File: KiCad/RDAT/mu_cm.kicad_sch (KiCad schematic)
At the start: 9 parts

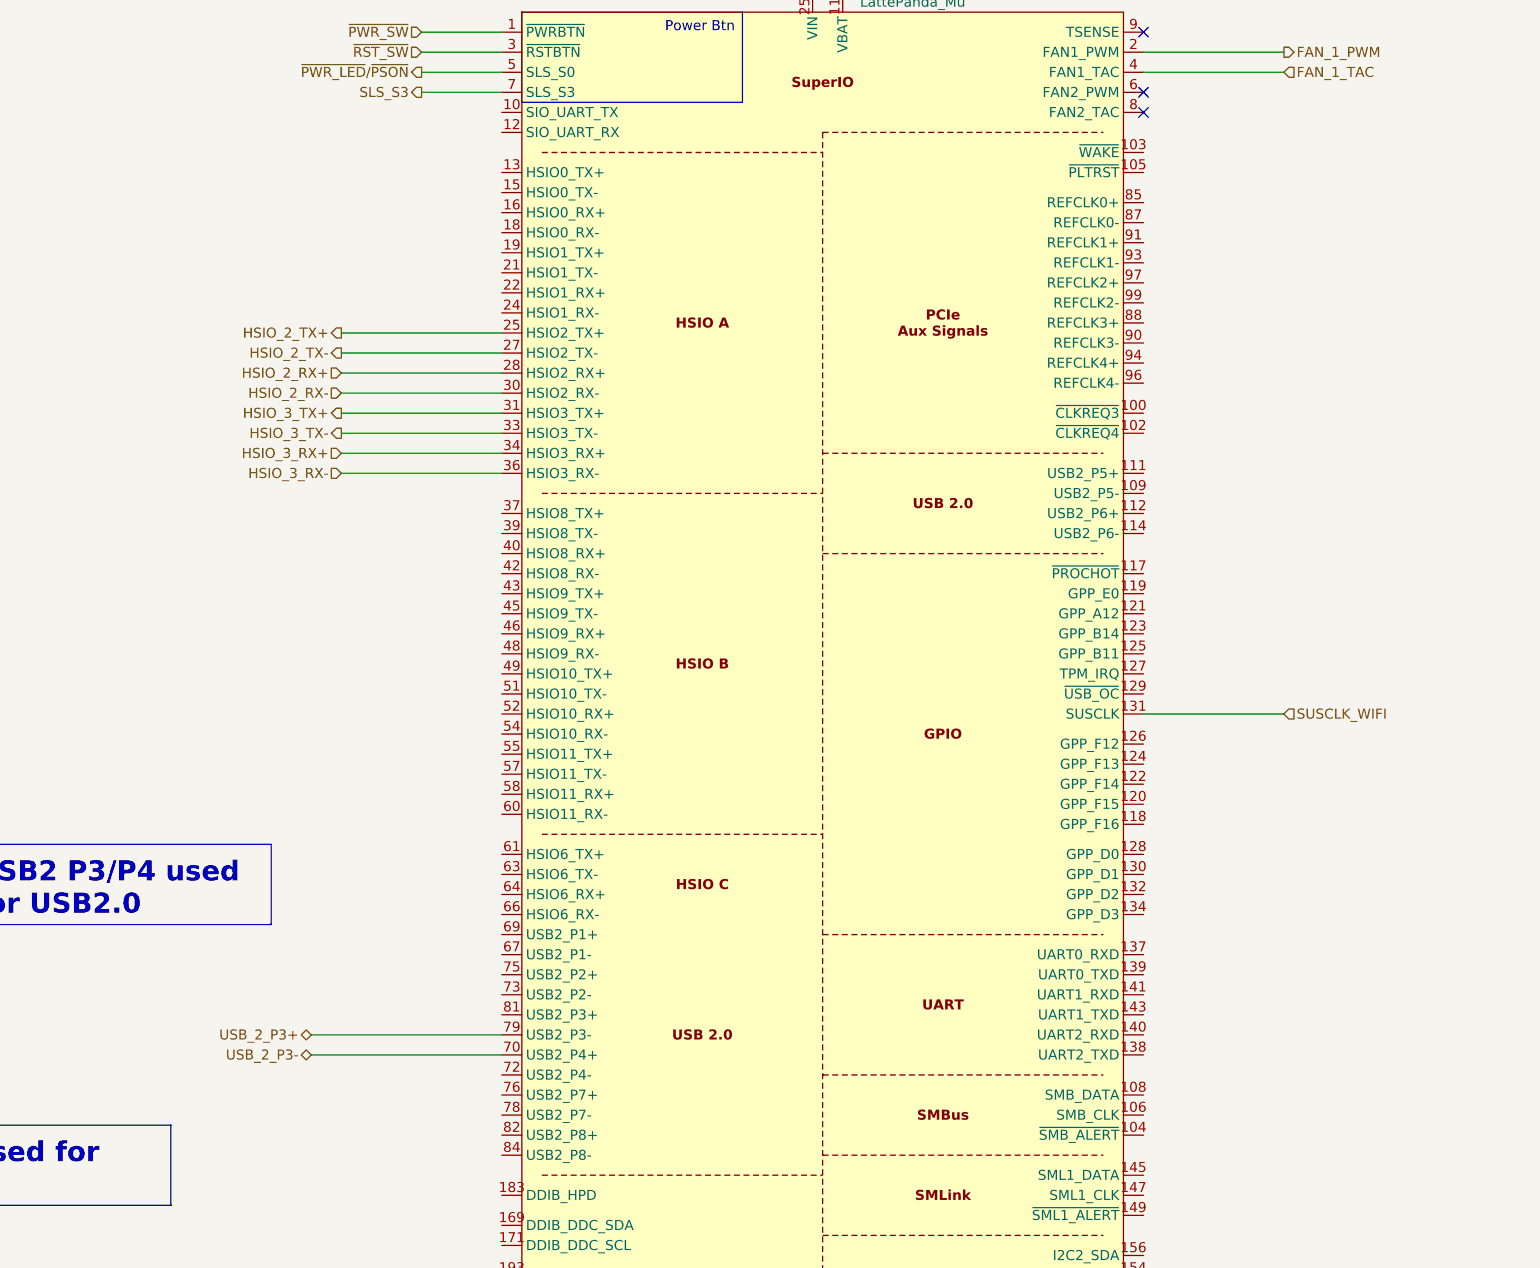
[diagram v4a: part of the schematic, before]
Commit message: Connected m.2 E Key
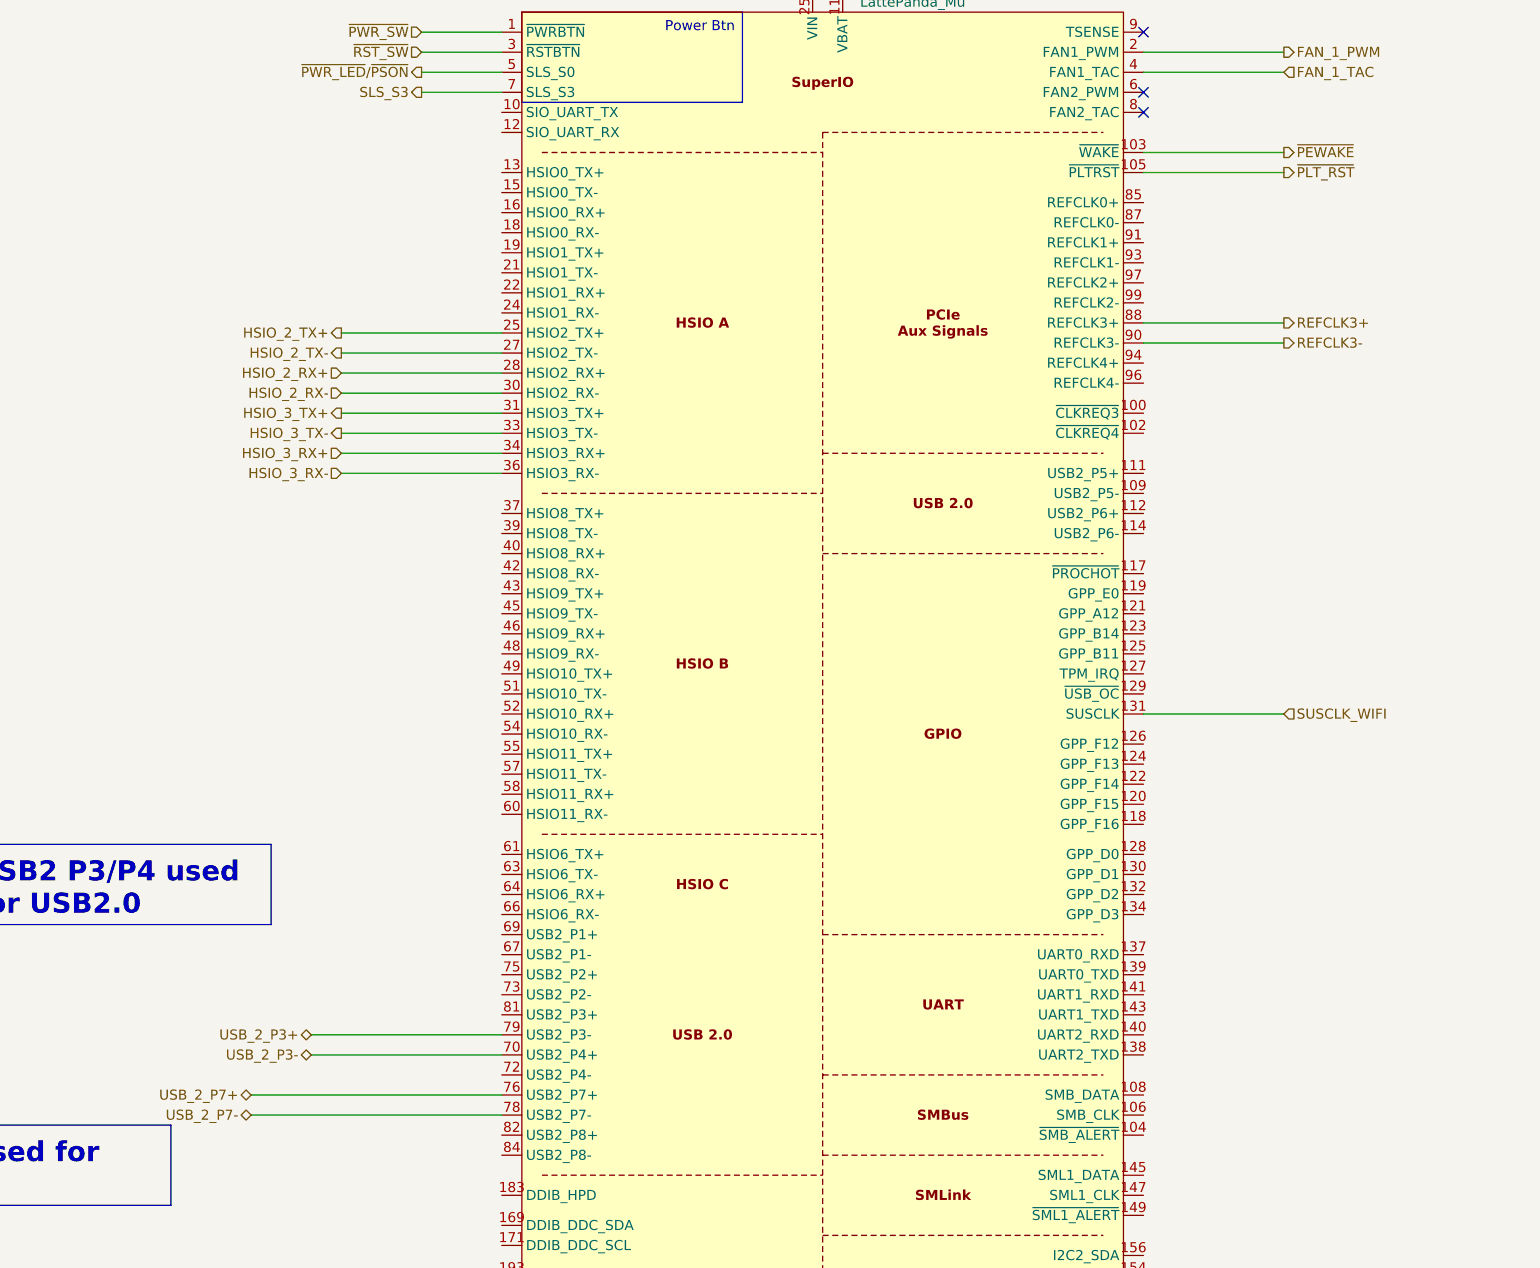
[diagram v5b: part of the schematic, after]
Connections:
- net ~{PEWAKE}: now reaches A1.103 (~{WAKE})
- net ~{PLT_RST}: now reaches A1.105 (~{PLTRST})
- net USB_2_P7+: now reaches A1.76 (USB2_P7+)
- net USB_2_P7-: now reaches A1.78 (USB2_P7-)
- net REFCLK3+: now reaches A1.88 (REFCLK3+)
- net REFCLK3-: now reaches A1.90 (REFCLK3-)
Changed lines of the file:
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@@
+	(wire
+		(pts
+			(xy 176.53 104.14) (xy 194.31 104.14)
+		)
+		(stroke
+			(width 0)
+			(type default)
+		)
+	)
 	(wire
 		(pts
@@
 	(wire
 		(pts
+			(xy 95.25 201.93) (xy 63.5 201.93)
+		)
+		(stroke
+			(width 0)
+			(type default)
+		)
+	)
+	(wire
+		(pts
 			(xy 181.61 262.89) (xy 184.15 262.89)
 		)
@@
 	(wire
 		(pts
+			(xy 176.53 106.68) (xy 194.31 106.68)
+		)
+		(stroke
+			(width 0)
+			(type default)
+		)
+	)
+	(wire
+		(pts
 			(xy 85.09 67.31) (xy 95.25 67.31)
 		)
@@
 	(wire
 		(pts
+			(xy 176.53 85.09) (xy 194.31 85.09)
+		)
+		(stroke
+			(width 0)
+			(type default)
+		)
+	)
+	(wire
+		(pts
 			(xy 63.5 237.49) (xy 95.25 237.49)
 		)
@@
 	(wire
 		(pts
+			(xy 95.25 204.47) (xy 63.5 204.47)
+		)
+		(stroke
+			(width 0)
+			(type default)
+		)
+	)
+	(wire
+		(pts
 			(xy 74.93 118.11) (xy 95.25 118.11)
 		)
@@
 	(wire
 		(pts
+			(xy 176.53 82.55) (xy 194.31 82.55)
+		)
+		(stroke
+			(width 0)
+			(type default)
+		)
+	)
+	(wire
+		(pts
 			(xy 148.59 49.53) (xy 157.48 49.53)
 		)
@@
 		)
 	)
+	(hierarchical_label "~{PLT_RST}"
+		(shape output)
+		(at 194.31 85.09 0)
+		(effects
+			(font
+				(size 1.27 1.27)
+			)
+			(justify left)
+		)
+	)
 	(hierarchical_label "FAN_1_TAC"
 		(shape input)
@@
 		)
 	)
+	(hierarchical_label "~{PEWAKE}"
+		(shape output)
+		(at 194.31 82.55 0)
+		(effects
+			(font
+				(size 1.27 1.27)
+			)
+			(justify left)
+		)
+	)
 	(hierarchical_label "DDI_B_TX2+"
 		(shape output)
@@
 			)
 			(justify left)
+		)
+	)
+	(hierarchical_label "USB_2_P7-"
+		(shape bidirectional)
+		(at 63.5 204.47 180)
+		(effects
+			(font
+				(size 1.27 1.27)
+			)
+			(justify right)
 		)
 	)
@@
 		)
 	)
+	(hierarchical_label "REFCLK3-"
+		(shape output)
+		(at 194.31 106.68 0)
+		(effects
+			(font
+				(size 1.27 1.27)
+			)
+			(justify left)
+		)
+	)
 	(hierarchical_label "HSIO_3_RX+"
 		(shape input)
@@
 		(shape output)
 		(at 63.5 242.57 180)
+		(effects
+			(font
+				(size 1.27 1.27)
+			)
+			(justify right)
+		)
+	)
+	(hierarchical_label "USB_2_P7+"
+		(shape bidirectional)
+		(at 63.5 201.93 180)
 		(effects
 			(font
@@
 		)
 	)
+	(hierarchical_label "REFCLK3+"
+		(shape output)
+		(at 194.31 104.14 0)
+		(effects
+			(font
+				(size 1.27 1.27)
+			)
+			(justify left)
+		)
+	)
